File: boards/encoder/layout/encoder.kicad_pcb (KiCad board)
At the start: 2 copper layers, 9.6 x 14.1 mm, 3 parts, among them IC1 AS5047U-HTSM, J1 EncoderTab

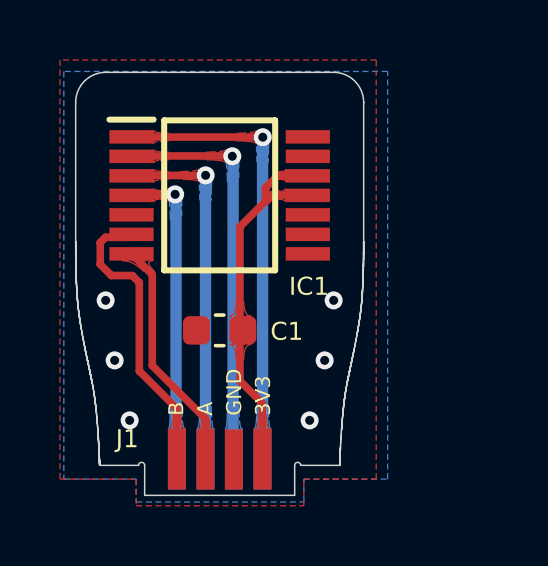
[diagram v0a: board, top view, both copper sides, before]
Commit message: ✨ Pull the AS5047U's SPI inputs on the encoder board
AS5047U DS v1-00 Figure 4 note 1 forbids a floating digital input, and
CSn, CLK and MOSI float while the main board's MCU is in reset (its pins
are in analog mode, RM0468 section 11.3.1). The board now carries the
pulls of notes 2 and 3, with the part that needs them:

- R1 10 kOhm, Encoder_CSn to 3V3: the sensor stays deselected.
- R2 100 kOhm, SPI_SCK to GND, and R3 100 kOhm, SPI_MOSI to GND: the
  lines idle low (SPI mode 1). Both encoder boards and the IMU share
  them, so the two boards' pull-downs act in parallel (50 kOhm, 66 uA
  with a line high); the LSM6DSV adds no pull-up (DS13476 Table 22).

Uni-Royal 0402 1 % parts, JLCPCB basic, already in parts/jlc.toml.
changes.toml declares the three parts for the previous-revision gate,
the board bench checks the pulls and their range (spi_inputs_held), and
the pytests compare the netlist with the previous revision plus the
declared change. transfer_layout.py leaves parts the previous board does
not have where the netlist sync puts them; the next commit places them.
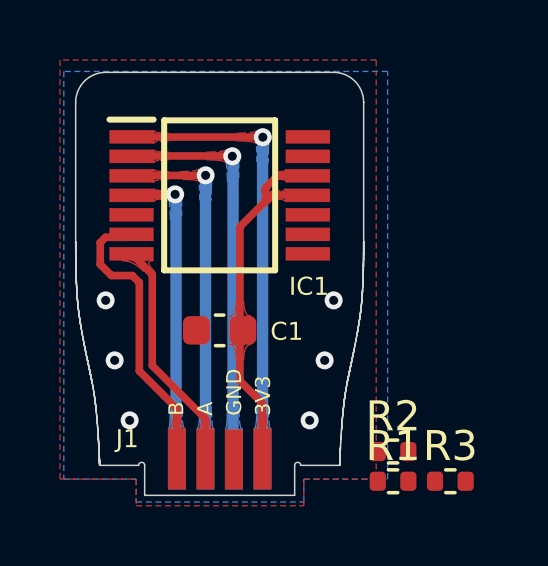
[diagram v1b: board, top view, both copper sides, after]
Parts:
- added R1: 10k 1%, stdlib_kicad-footprints_Resistor_SMD:R_0402_1005Metric, F.Cu at (154.3, 111.6)
- added R2: 100k 1%, stdlib_kicad-footprints_Resistor_SMD:R_0402_1005Metric, F.Cu at (154.3, 110.6)
- added R3: 100k 1%, stdlib_kicad-footprints_Resistor_SMD:R_0402_1005Metric, F.Cu at (156.2, 111.6)

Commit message: 🐛 Fix the encoder layout's DRC findings and place R1-R3
boards/encoder/layout/fixes.py, a one-off pcbnew script run on the
previous layout after the netlist sync added R1-R3:

- Outline: delete the 1 nm Edge.Cuts line the Altium conversion left at
  the top right corner, KiCad (153.3011, 98.953604)-(153.3011,
  98.953605), and start the right side on the corner arc's end
  (invalid_outline). The outline is unchanged; micras-pcb mech still
  matches spec/encoder.toml.
- Teardrops: delete the second SPI_MOSI teardrop at IC1 pad 4, which
  overlapped the first and left a copper sliver (copper_sliver). Pad 4
  keeps one teardrop, as pads 1-3.
- Supply: 3V3 runs straight up from its tab pad to IC1 pins 11/12 over
  the bottom-side Encoder_CSn track, freeing the top side above SPI_SCK
  and SPI_MOSI. C1 sits on it right below IC1, 4.0 mm from pin 11 (pad
  centres; 5.0 mm before). One stitching via moves 0.15 mm out, clear
  of C1's GND pad.
- R3 and R2 sit above the SPI_MOSI and SPI_SCK bottom tracks with a via
  onto each; R1 sits right of the 3V3 track with a via and a short
  bottom-side track to Encoder_CSn.
- Silkscreen: IC1's designator above the package, C1's below its GND
  pad; R1-R3 keep theirs on F.Fab (no room for 0.1 mm silk clearance).

New items take UUIDs from a seeded generator: transfer_layout.py, then
fixes.py, then make gen rebuild this layout byte for byte. Encoder DRC
and DFM are clean.
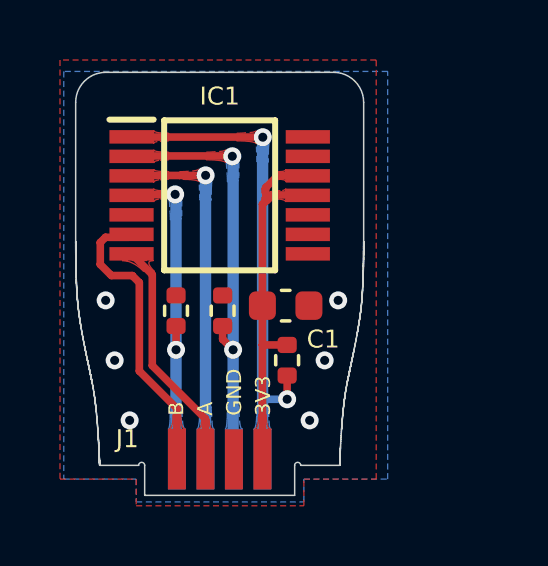
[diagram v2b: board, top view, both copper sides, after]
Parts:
- moved R3 10.8 mm to (147.0, 105.9), turned to 90 degrees
- moved R2 7.37 mm to (148.6, 105.9), turned to 90 degrees
- moved R1 5.36 mm to (150.8, 107.5), turned to -90 degrees
- moved C1 2.35 mm to (150.7, 105.7), turned to 0 degrees
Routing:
- net Encoder_CSn: track 15.2 -> 16.8 mm, vias 1 -> 2
- net SPI_SCK: track 13.5 -> 14.4 mm, vias 1 -> 2
- net SPI_MOSI: track 10.3 -> 11.1 mm, vias 1 -> 2
